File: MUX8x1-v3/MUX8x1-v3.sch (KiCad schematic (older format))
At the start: 38 parts, among them J1 Conn_01x09_Male, J10 Conn_01x03_Male, J11 Conn_01x09_Male, J12 Conn_01x09_Male, J14 Conn_01x09_Male, J15 Conn_01x09_Male, J16 Conn_01x09_Male, J18 Conn_01x09_Male, J19 Conn_01x09_Male, J2 Conn_01x09_Male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

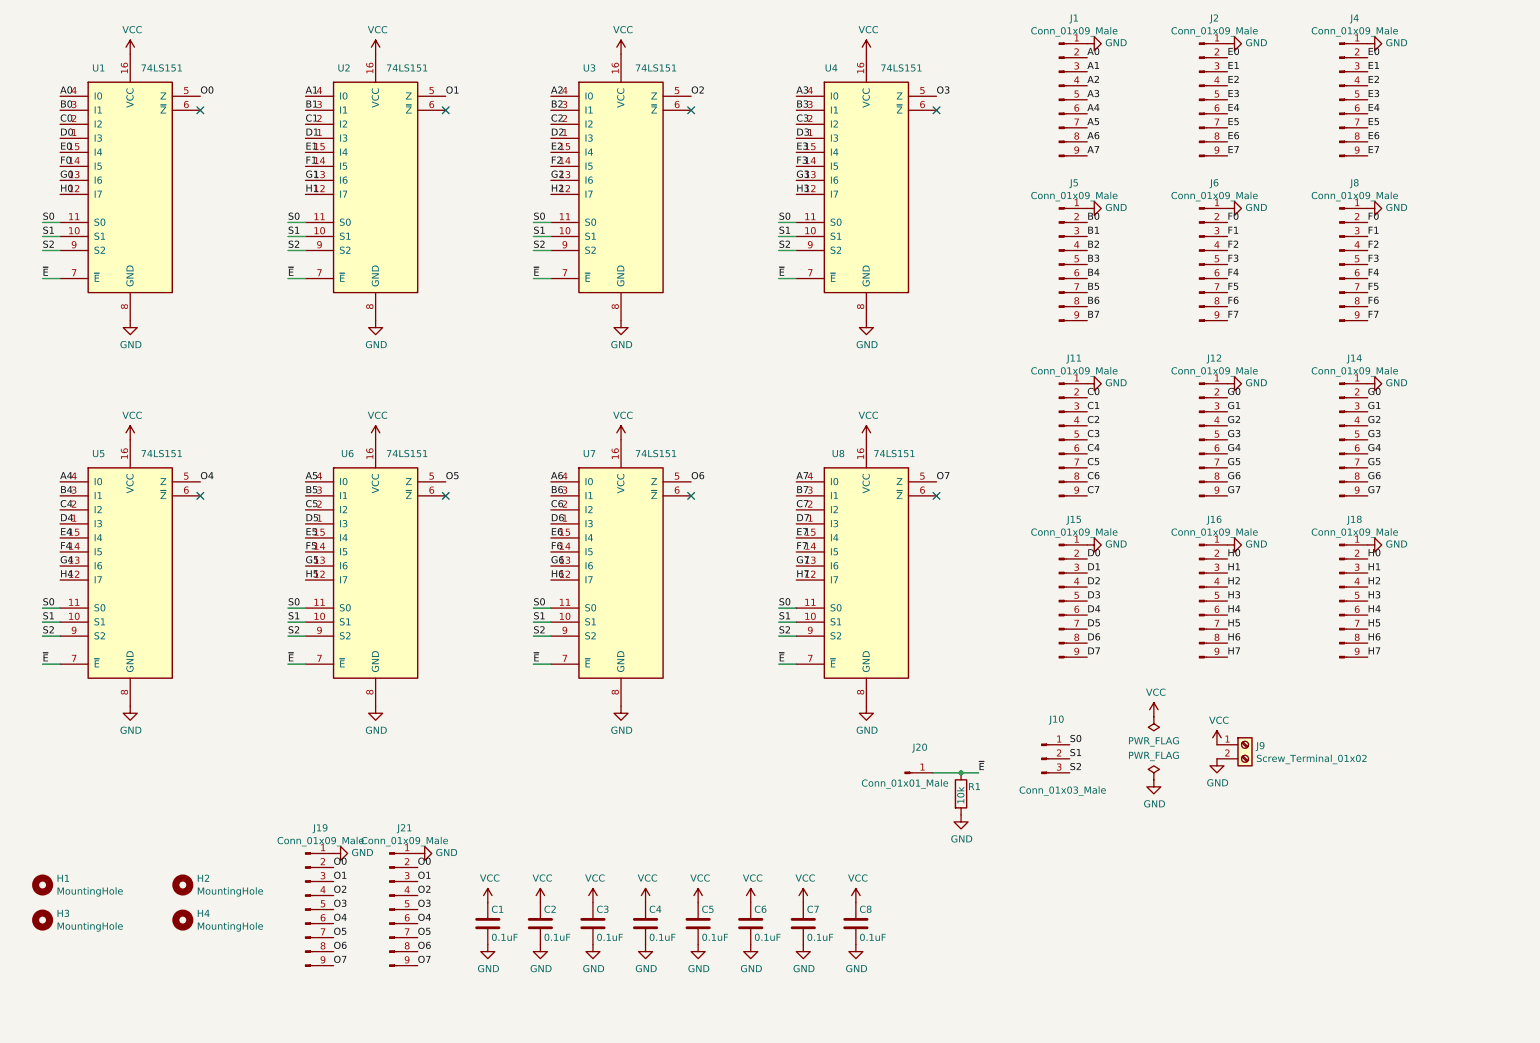
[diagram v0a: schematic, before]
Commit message: MUX8:1 remake
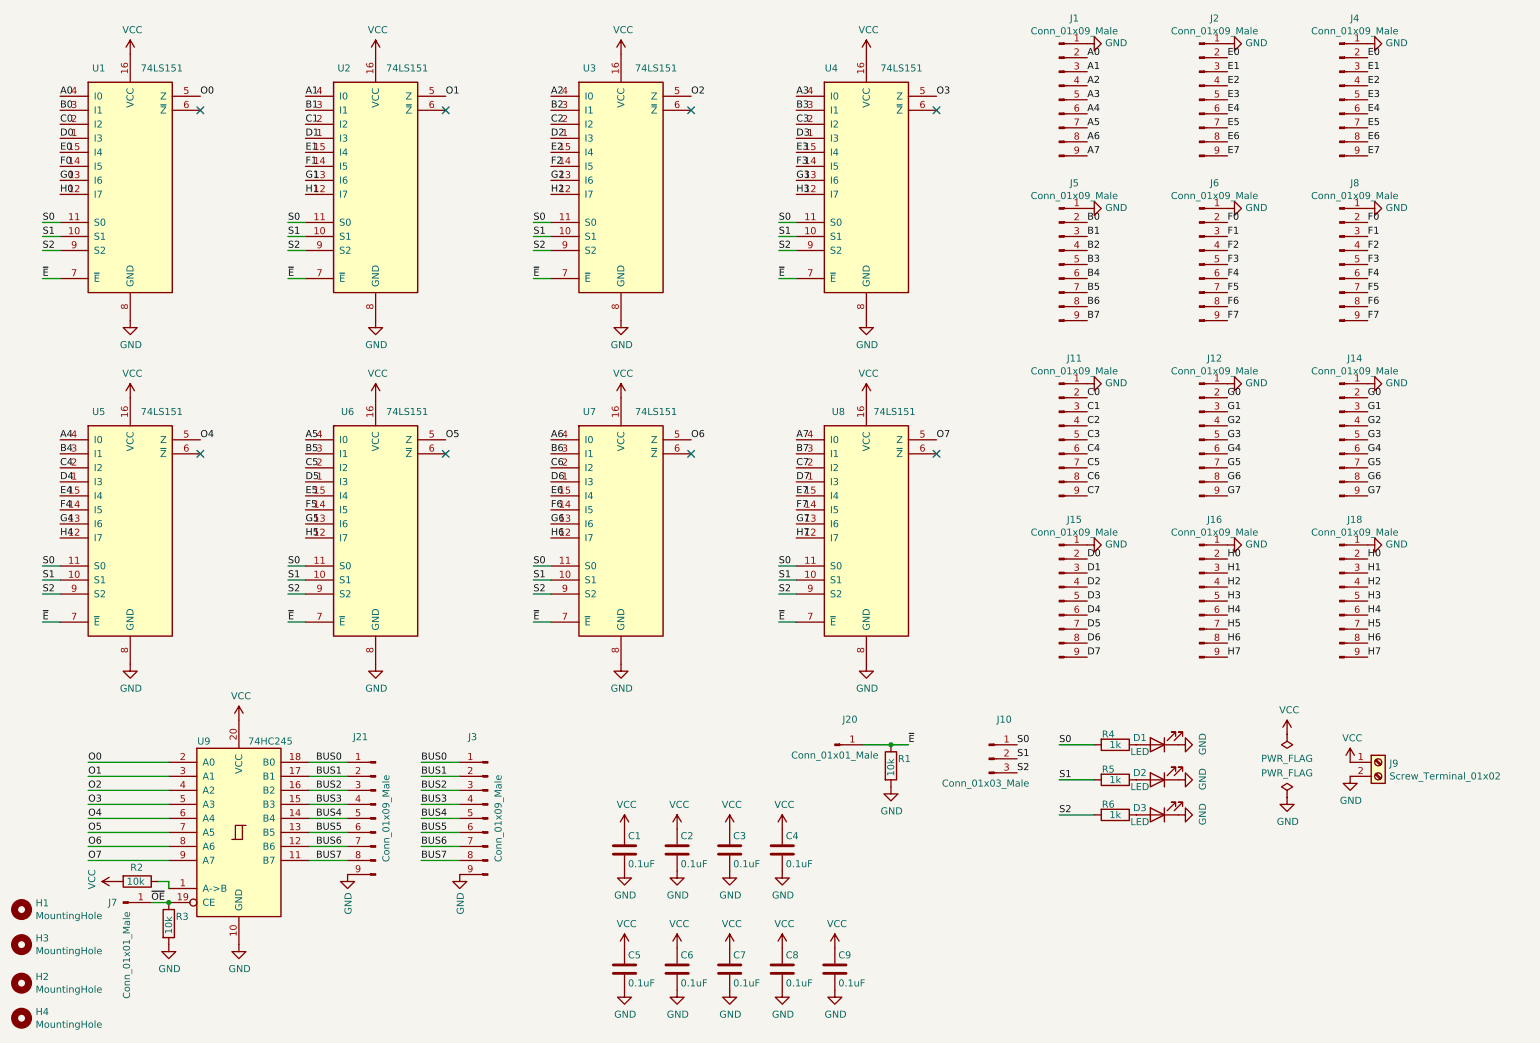
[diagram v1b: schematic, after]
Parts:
- removed J19: Conn_01x09_Male, Connector_PinHeader_2.54mm:PinHeader_1x09_P2.54mm_Vertical, symbol Connector:Conn_01x09_Male
- added C9: 0.1uF, Capacitor_THT:C_Axial_L5.1mm_D3.1mm_P15.00mm_Horizontal, symbol Device:C
- added D1, D2, D3: LED, LED_SMD:LED_0805_2012Metric_Pad1.15x1.40mm_HandSolder, symbol Device:LED
- added J3: Conn_01x09_Male, Connector_PinHeader_2.54mm:PinHeader_1x09_P2.54mm_Vertical, symbol Connector:Conn_01x09_Male
- added J7: Conn_01x01_Male, Connector_PinHeader_2.54mm:PinHeader_1x01_P2.54mm_Vertical, symbol Connector:Conn_01x01_Male
- added R2, R3: 10k, Resistor_SMD:R_0805_2012Metric_Pad1.20x1.40mm_HandSolder, symbol Device:R
- added R4, R5, R6: 1k, Resistor_SMD:R_0805_2012Metric_Pad1.20x1.40mm_HandSolder, symbol Device:R
- added U9: 74HC245, Package_DIP:DIP-20_W7.62mm_Socket, symbol 74xx:74HC245
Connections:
- net GND: now also J21.9 (Pin_9), C9.2, D1.1 (K), D2.1 (K), D3.1 (K), J3.9 (Pin_9), R3.2, U9.10 (GND); no longer J21.1 (Pin_1)
- net O0: now also U9.2 (A0); no longer J21.2 (Pin_2)
- net O1: now also U9.3 (A1); no longer J21.3 (Pin_3)
- net O2: now also U9.4 (A2); no longer J21.4 (Pin_4)
- net O3: now also U9.5 (A3); no longer J21.5 (Pin_5)
- net O4: now also U9.6 (A4); no longer J21.6 (Pin_6)
- net O5: now also U9.7 (A5); no longer J21.7 (Pin_7)
- net O6: now also U9.8 (A6); no longer J21.8 (Pin_8)
- net O7: now also U9.9 (A7); no longer J21.9 (Pin_9)
- net S0: now also R4.2
- net S1: now also R5.2
- net S2: now also R6.2
- net VCC: now also C9.1, R2.2, U9.20 (VCC)
- new net: R2.1, U9.1 (A->B)
- new net: D1.2 (A), R4.1
- new net: D2.2 (A), R5.1
- new net: D3.2 (A), R6.1
- new net BUS0: J21.1 (Pin_1), J3.1 (Pin_1), U9.18 (B0)
- new net BUS1: J21.2 (Pin_2), J3.2 (Pin_2), U9.17 (B1)
- new net BUS2: J21.3 (Pin_3), J3.3 (Pin_3), U9.16 (B2)
- new net BUS3: J21.4 (Pin_4), J3.4 (Pin_4), U9.15 (B3)
- new net BUS4: J21.5 (Pin_5), J3.5 (Pin_5), U9.14 (B4)
- new net BUS5: J21.6 (Pin_6), J3.6 (Pin_6), U9.13 (B5)
- new net BUS6: J21.7 (Pin_7), J3.7 (Pin_7), U9.12 (B6)
- new net BUS7: J21.8 (Pin_8), J3.8 (Pin_8), U9.11 (B7)
- new net ~OE: J7.1 (Pin_1), R3.1, U9.19 (CE)
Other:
- moved on the sheet: C1, C2, C3, C4, C5, C6, C7, C8, H1, H2, H3, H4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
